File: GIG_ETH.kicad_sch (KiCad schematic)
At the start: 9 parts, among them U11 RTL8211F-CG

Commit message: Stuff
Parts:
- removed unit 2 of U11
- added R41, R42, R43, R44: 4K7, Resistor_SMD:R_0402_1005Metric_Pad0.72x0.64mm_HandSolder, symbol Device:R
- added R45, R46, R47, R48: 22, Resistor_SMD:R_0402_1005Metric_Pad0.72x0.64mm_HandSolder, symbol Device:R
- R20, R33, R34, R35, R36, R37, R38, R39: footprint (none) -> Resistor_SMD:R_0402_1005Metric_Pad0.72x0.64mm_HandSolder
- U11: footprint RTL8211F-CG_RTK -> lib:RTL8211F-CG_RTK
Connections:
- net 1V8_ETH: now also R41.1, R42.1, R43.1, R44.1
- net ETH_RXD2: now also R37.2
- net ETH_RXD3: no longer R37.2
- net ETH_TXD0: now also R44.2, R45.1; no longer U11.18 (TXD0)
- net ETH_TXD1: now also R43.2, R46.1; no longer U11.17 (TXD1)
- net ETH_TXD2: now also R42.2, R47.1; no longer U11.16 (TXD2)
- net ETH_TXD3: now also R41.2, R48.1; no longer U11.15 (TXD3)
- new net: R46.2, U11.17 (TXD1)
- new net: R48.2, U11.15 (TXD3)
- new net: R47.2, U11.16 (TXD2)
- new net: R45.2, U11.18 (TXD0)

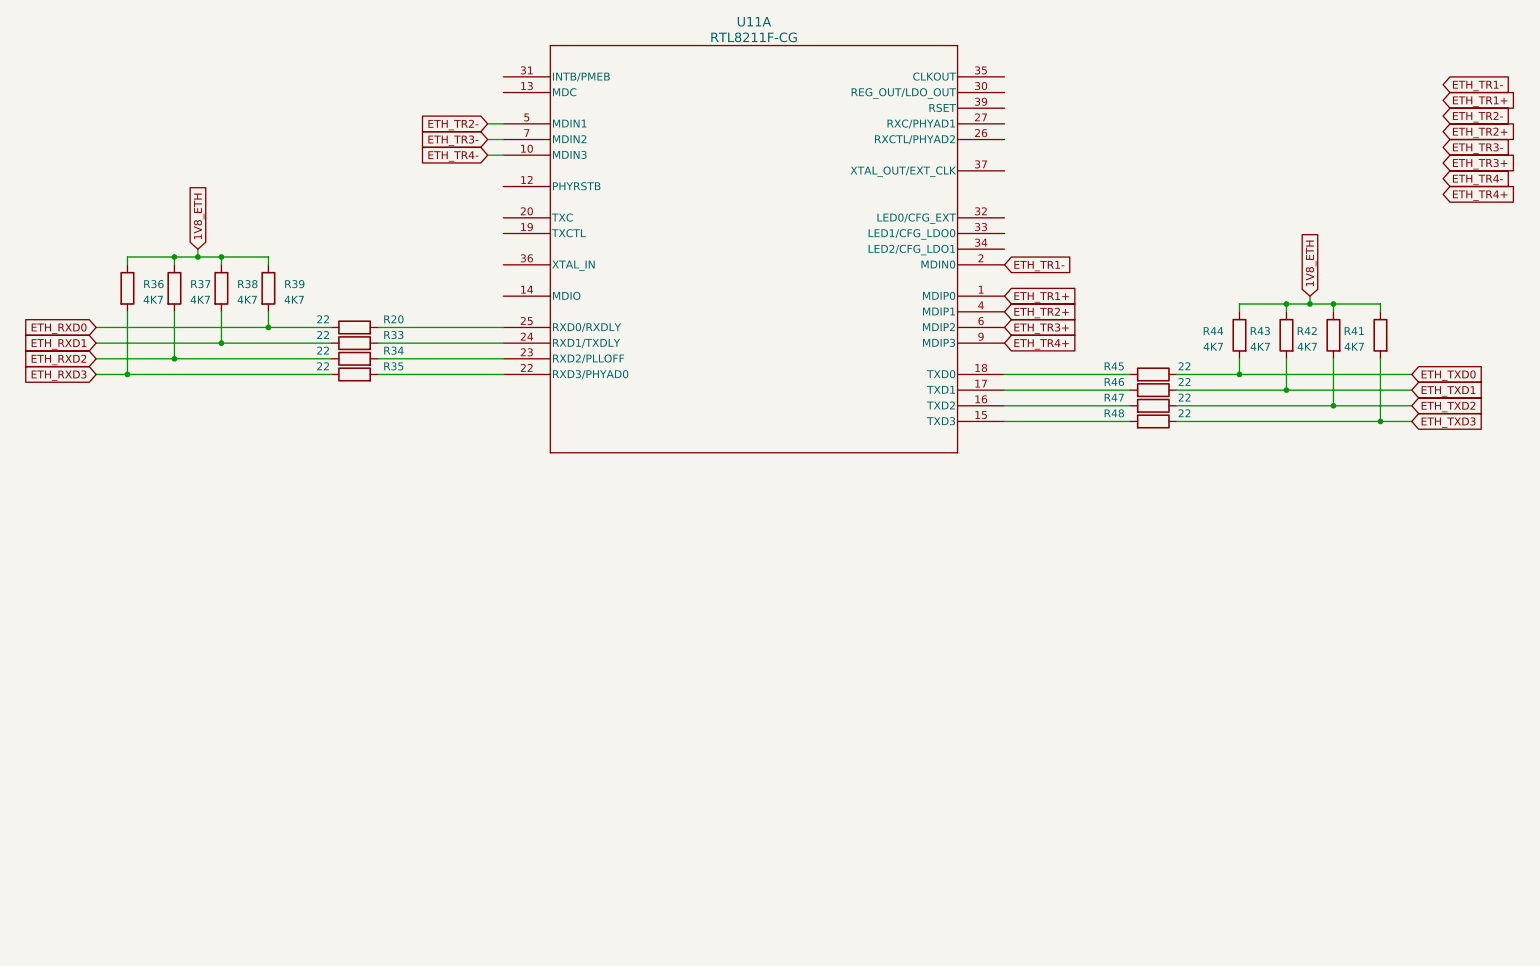
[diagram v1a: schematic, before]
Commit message: Gbe routing
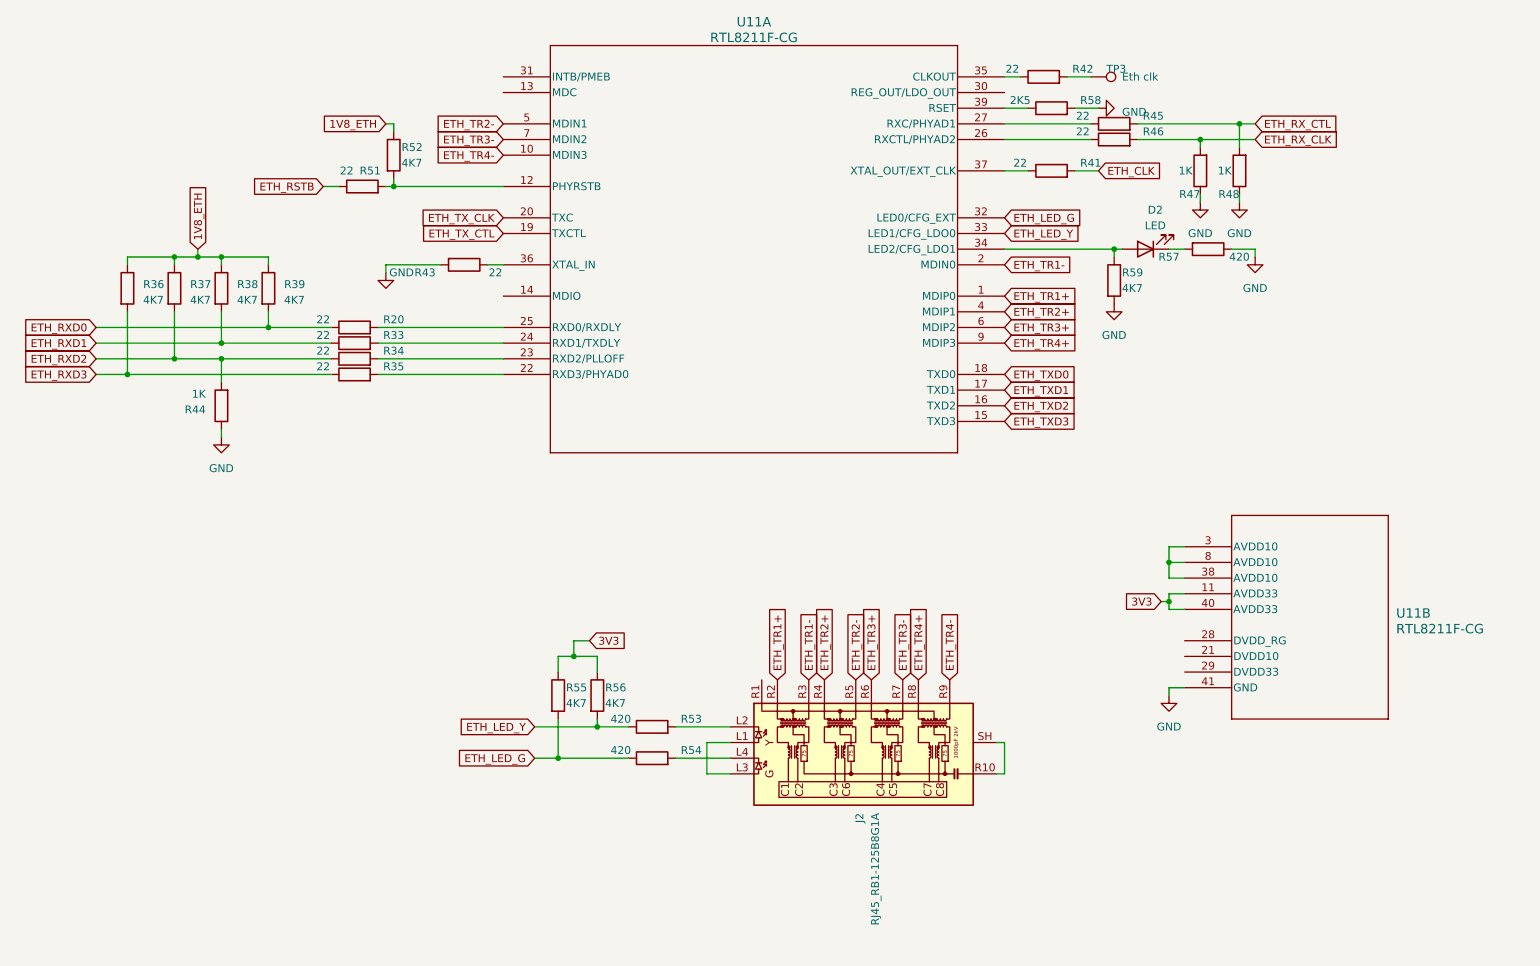
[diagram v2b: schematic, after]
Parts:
- added D2: LED, symbol Device:LED
- added J2: RJ45_RB1-125B8G1A, Connector_RJ:RJ45_UDE_RB1-125B8G1A, symbol Connector:RJ45_RB1-125B8G1A
- added R51: 22, Resistor_SMD:R_0402_1005Metric_Pad0.72x0.64mm_HandSolder, symbol Device:R
- added R52, R55, R56, R59: 4K7, Resistor_SMD:R_0402_1005Metric_Pad0.72x0.64mm_HandSolder, symbol Device:R
- added R53, R54, R57: 420, Resistor_SMD:R_0402_1005Metric_Pad0.72x0.64mm_HandSolder, symbol Device:R
- added R58: 2K5, Resistor_SMD:R_0402_1005Metric_Pad0.72x0.64mm_HandSolder, symbol Device:R
- added TP3: Eth clk, TestPoint:TestPoint_Pad_D1.0mm, symbol Connector:TestPoint
- added unit 2 of U11
- R41, R42, R43: value 4K7 -> 22
- R44: value 4K7 -> 1K
- R47, R48: value 22 -> 1K
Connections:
- net 1V8_ETH: now also R52.1; no longer R41.1, R42.1, R43.1, R44.1
- net ETH_RXD2: now also R44.2
- net ETH_TR1+: now also J2.R2 (TD1+)
- net ETH_TR1-: now also J2.R3 (TD1-)
- net ETH_TR2+: now also J2.R4 (TD2+)
- net ETH_TR2-: now also J2.R5 (TD2-)
- net ETH_TR3+: now also J2.R6 (TD3+)
- net ETH_TR3-: now also J2.R7 (TD3-)
- net ETH_TR4+: now also J2.R8 (TD4+)
- net ETH_TR4-: now also J2.R9 (TD4-)
- net ETH_TXD0: now also U11.18 (TXD0); no longer R44.2, R45.1
- net ETH_TXD1: now also U11.17 (TXD1); no longer R43.2, R46.1
- net ETH_TXD2: now also U11.16 (TXD2); no longer R42.2, R47.1
- net ETH_TXD3: now also U11.15 (TXD3); no longer R41.2, R48.1
- net ETH_RX_CLK: now reaches R46.2
- net ETH_RX_CLK: now also R47.2; no longer U11.17 (TXD1)
- net at U11.12 (PHYRSTB): now also R51.2, R52.2
- net ETH_RX_CTL: now reaches R48.2
- net ETH_RX_CTL: now also R45.2; no longer U11.15 (TXD3)
- net ETH_TX_CTL: now reaches U11.19 (TXCTL)
- net ETH_TX_CLK: now reaches U11.20 (TXC)
- net at U11.26 (RXCTL/PHYAD2): now also R46.1
- net at U11.27 (RXC/PHYAD1): now also R45.1
- net ETH_LED_G: now reaches U11.32 (LED0/CFG_EXT)
- net ETH_LED_G: now also R54.1, R55.2
- net ETH_LED_Y: now reaches U11.33 (LED1/CFG_LDO0)
- net ETH_LED_Y: now also R53.1, R56.2
- net at U11.34 (LED2/CFG_LDO1): now also D2.2 (A), R59.1
- net at U11.35 (CLKOUT): now also R42.1
- net at U11.36 (XTAL_IN): now also R43.1
- net at U11.37 (XTAL_OUT/EXT_CLK): now also R41.1
- net at U11.39 (RSET): now also R58.1
- new net: D2.1 (K), R57.2
- new net: R42.2, TP3.1
- new net: J2.L2, R53.2
- new net: J2.L1, J2.L3
- new net: J2.L4, R54.2
- new net: J2.R10 (GND), J2.SH
- new net: U11.3 (AVDD10), U11.38 (AVDD10), U11.8 (AVDD10)
- new net 3V3: R55.1, R56.1, U11.11 (AVDD33), U11.40 (AVDD33)
- new net ETH_CLK: R41.2
- new net ETH_RSTB: R51.1
- new net GND: R43.2, R44.1, R47.1, R48.1, R57.1, R58.2, R59.2, U11.41 (GND)

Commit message: stuff
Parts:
- D2: footprint (none) -> LED_SMD:LED_0603_1608Metric_Pad1.05x0.95mm_HandSolder
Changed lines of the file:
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@@
       (effects (font (size 1.27 1.27)))
     )
-    (property "Footprint" "" (at 200.66 78.74 0)
+    (property "Footprint" "LED_SMD:LED_0603_1608Metric_Pad1.05x0.95mm_HandSolder" (at 200.66 78.74 0)
       (effects (font (size 1.27 1.27)) hide)
     )
